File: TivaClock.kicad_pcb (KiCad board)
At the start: 2 copper layers, 6 parts, among them J1 Conn_01x10, J2 Conn_01x10, J3 Conn_01x10, J4 Conn_01x10, J5 Conn_01x20, J6 Conn_01x20

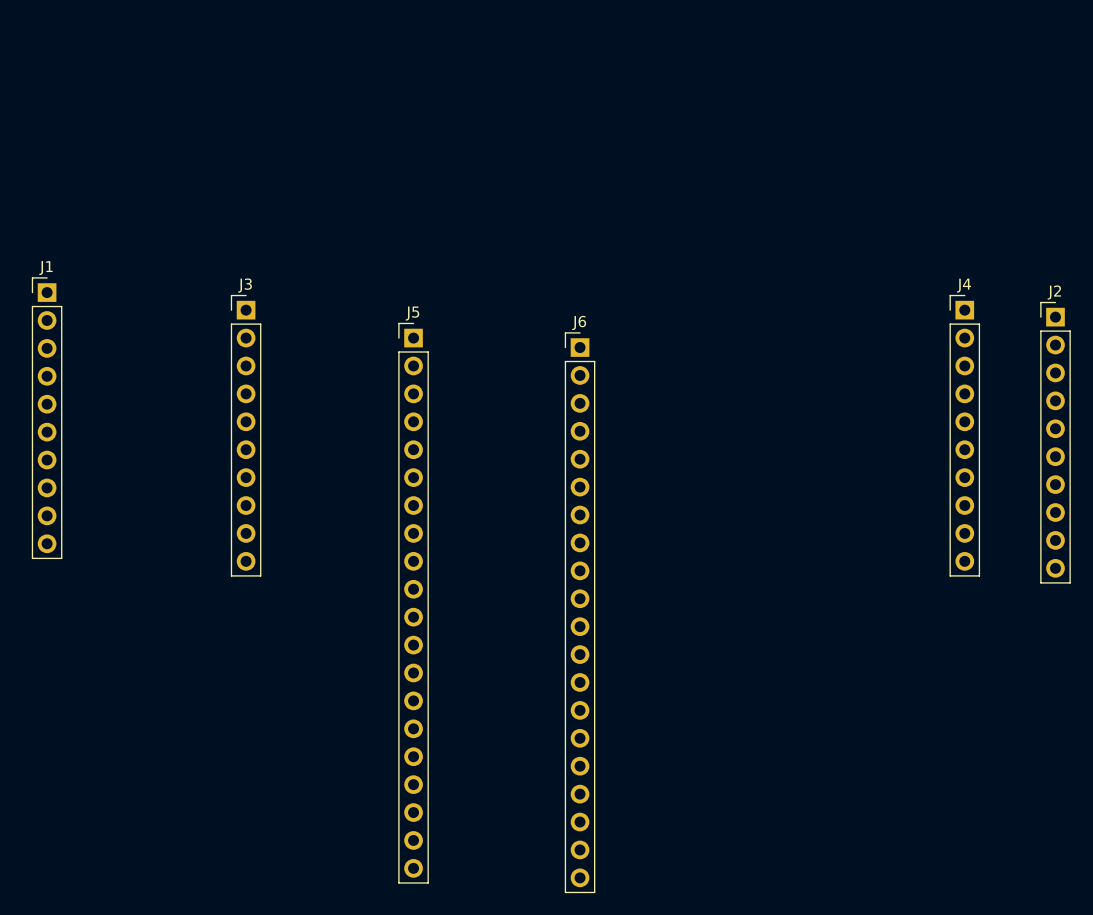
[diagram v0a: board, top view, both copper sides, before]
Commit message: added footprints and locations
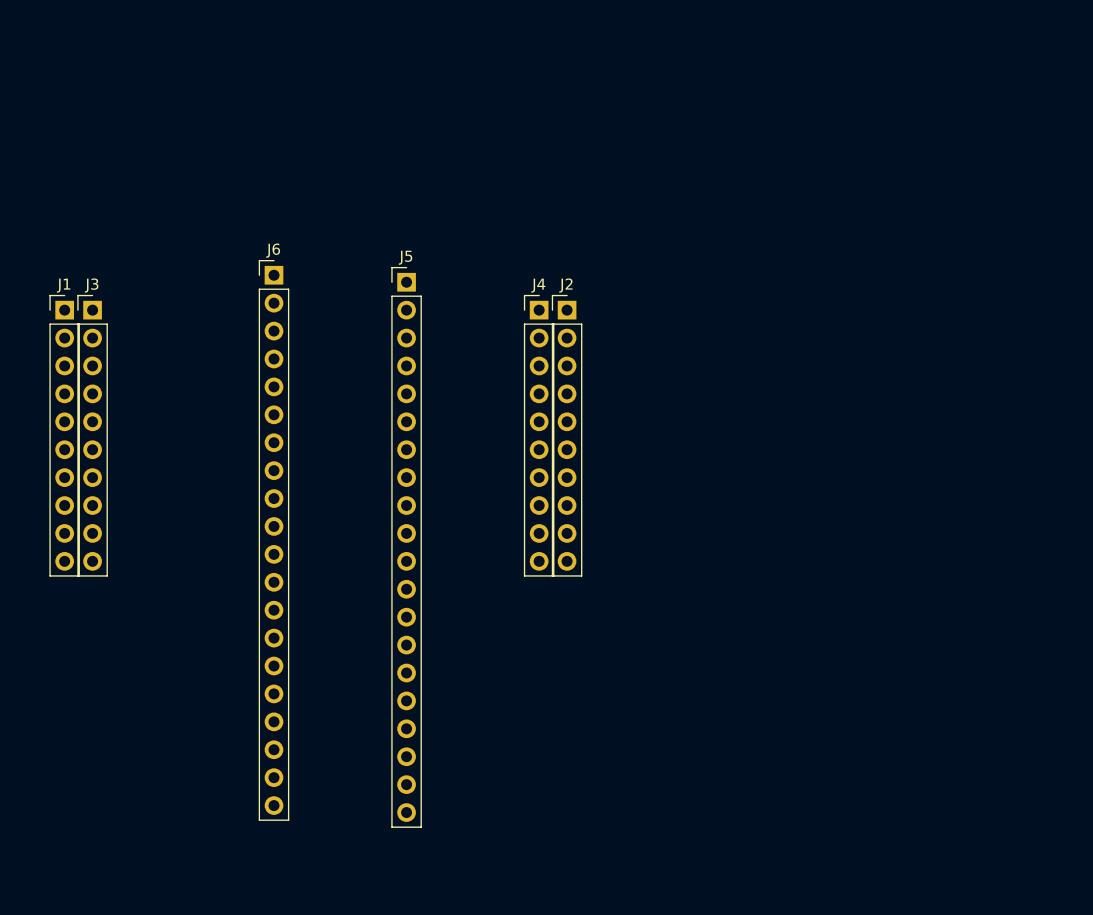
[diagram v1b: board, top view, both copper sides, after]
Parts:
- moved J2 44.5 mm to (147.3, 101.6)
- moved J4 38.7 mm to (144.8, 101.6)
- moved J6 28.6 mm to (120.7, 98.4)
- moved J3 14.0 mm to (104.1, 101.6)
- moved J5 5.12 mm to (132.7, 99.1)
- moved J1 2.26 mm to (101.6, 101.6)
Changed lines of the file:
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@@
   )
   (module Pin_Headers:Pin_Header_Straight_1x10_Pitch2.54mm (layer F.Cu)
-    (at 100 100)
+    (at 101.6 101.6)
     (descr "Through hole straight pin header, 1x10, 2.54mm pitch, single row")
     (tags "Through hole pin header THT 1x10 2.54mm single row")
@@
   )
   (module Pin_Headers:Pin_Header_Straight_1x10_Pitch2.54mm (layer F.Cu)
-    (at 191.77 102.235)
+    (at 147.32 101.6)
     (descr "Through hole straight pin header, 1x10, 2.54mm pitch, single row")
     (tags "Through hole pin header THT 1x10 2.54mm single row")
@@
   )
   (module Pin_Headers:Pin_Header_Straight_1x10_Pitch2.54mm (layer F.Cu)
-    (at 118.11 101.6)
+    (at 104.14 101.6)
     (descr "Through hole straight pin header, 1x10, 2.54mm pitch, single row")
     (tags "Through hole pin header THT 1x10 2.54mm single row")
@@
   )
   (module Pin_Headers:Pin_Header_Straight_1x10_Pitch2.54mm (layer F.Cu)
-    (at 183.515 101.6)
+    (at 144.78 101.6)
     (descr "Through hole straight pin header, 1x10, 2.54mm pitch, single row")
     (tags "Through hole pin header THT 1x10 2.54mm single row")
@@
   )
   (module Pin_Headers:Pin_Header_Straight_1x20_Pitch2.54mm (layer F.Cu)
-    (at 133.35 104.14)
+    (at 132.715 99.06)
     (descr "Through hole straight pin header, 1x20, 2.54mm pitch, single row")
     (tags "Through hole pin header THT 1x20 2.54mm single row")
@@
   )
   (module Pin_Headers:Pin_Header_Straight_1x20_Pitch2.54mm (layer F.Cu)
-    (at 148.5011 105.0036)
+    (at 120.65 98.425)
     (descr "Through hole straight pin header, 1x20, 2.54mm pitch, single row")
     (tags "Through hole pin header THT 1x20 2.54mm single row")

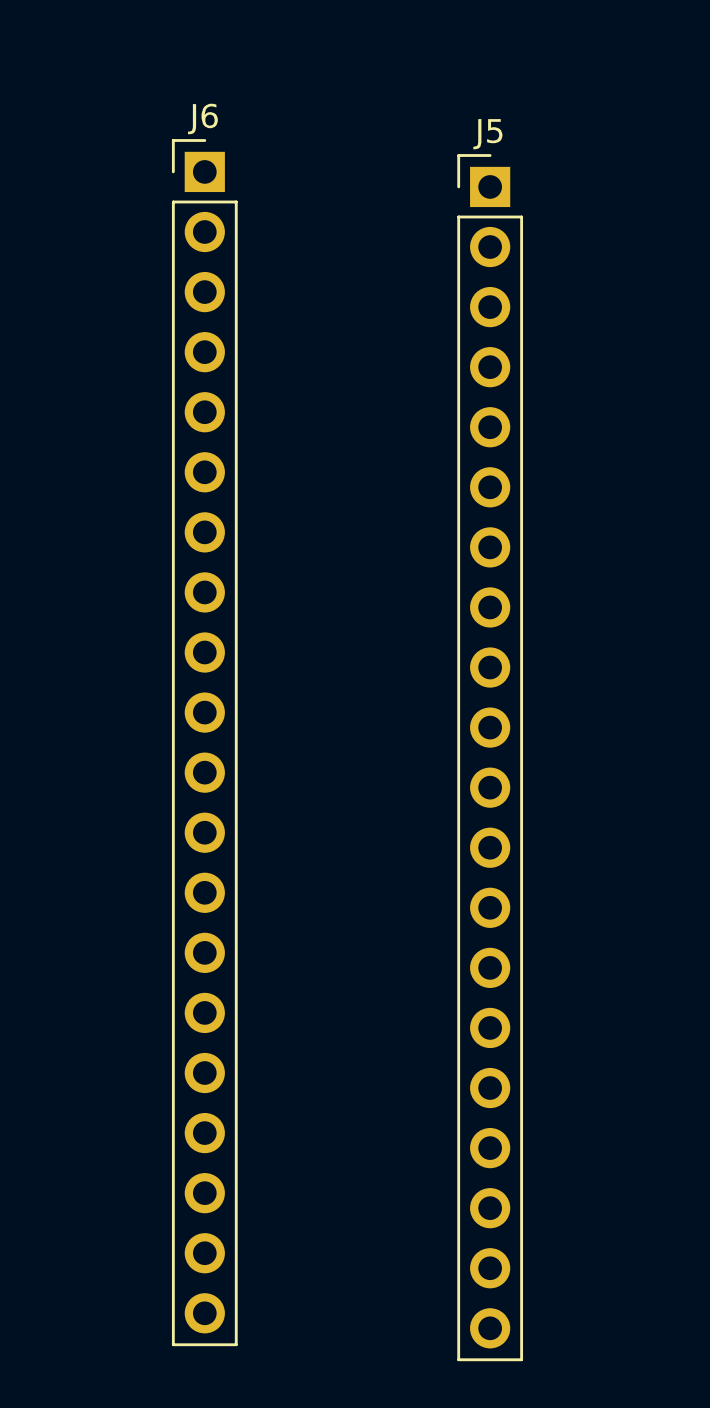
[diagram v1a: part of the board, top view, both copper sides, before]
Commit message: move clock micro to desired location
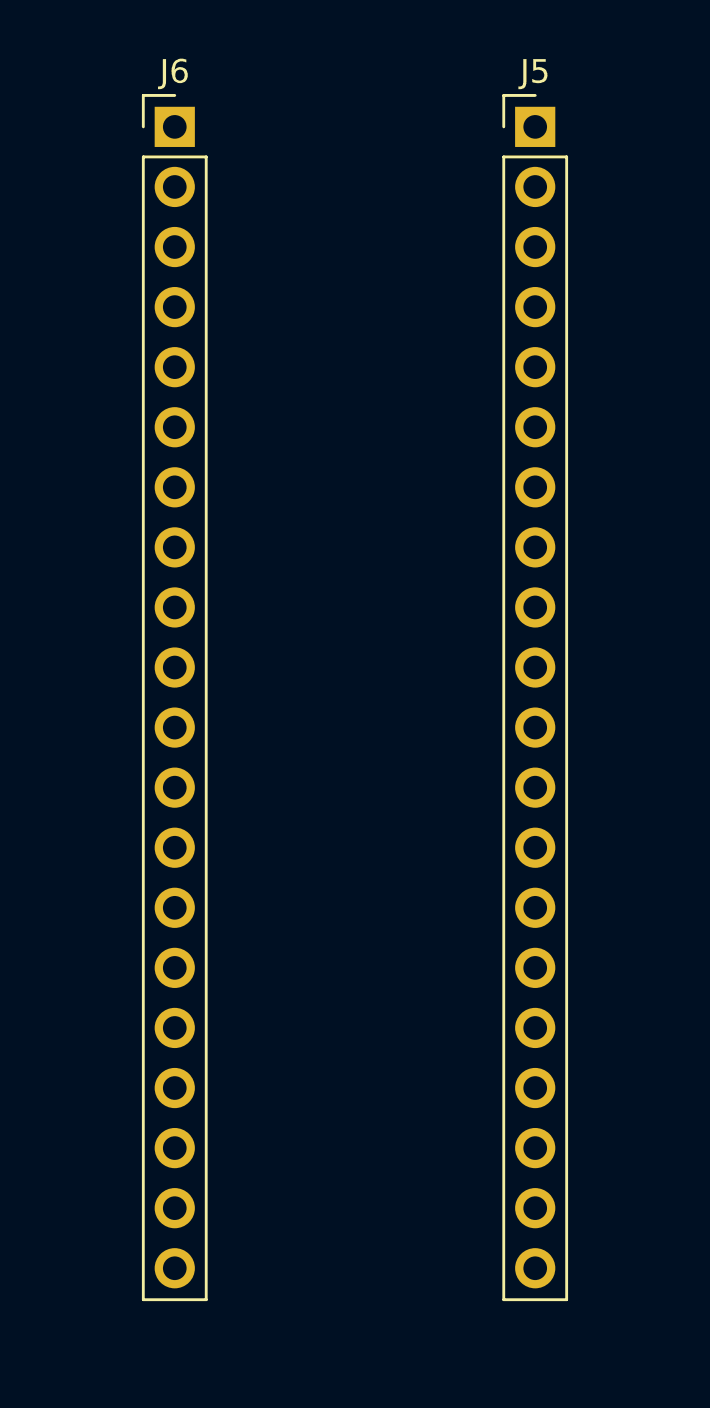
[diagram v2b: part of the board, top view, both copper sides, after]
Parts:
- moved J5 3.18 mm to (134.6, 96.5)
- moved J6 2.29 mm to (119.4, 96.5)
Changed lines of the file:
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@@
     (links 32)
     (no_connects 32)
-    (area 0 0 0 0)
+    (area 96.852381 95.12 152.06762 150.725)
     (thickness 1.6)
     (drawings 0)
@@
     (pad_to_mask_clearance 0.2)
     (aux_axis_origin 0 0)
+    (grid_origin 156.21 113.03)
     (visible_elements FFFFFF7F)
     (pcbplotparams
@@
   )
   (module Pin_Headers:Pin_Header_Straight_1x20_Pitch2.54mm (layer F.Cu)
-    (at 132.715 99.06)
+    (at 134.62 96.52)
     (descr "Through hole straight pin header, 1x20, 2.54mm pitch, single row")
     (tags "Through hole pin header THT 1x20 2.54mm single row")
@@
   )
   (module Pin_Headers:Pin_Header_Straight_1x20_Pitch2.54mm (layer F.Cu)
-    (at 120.65 98.425)
+    (at 119.38 96.52)
     (descr "Through hole straight pin header, 1x20, 2.54mm pitch, single row")
     (tags "Through hole pin header THT 1x20 2.54mm single row")

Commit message: orientate it corectly?
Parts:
- moved J5 30.5 mm to (134.6, 127.0), turned to 180 degrees
- moved J6 17.8 mm to (119.4, 78.7)
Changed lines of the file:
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@@
     (links 32)
     (no_connects 32)
-    (area 96.852381 95.12 152.06762 150.725)
+    (area 96.852381 75.435 152.06762 130.405)
     (thickness 1.6)
     (drawings 0)
@@
   )
   (module Pin_Headers:Pin_Header_Straight_1x20_Pitch2.54mm (layer F.Cu)
-    (at 134.62 96.52)
+    (at 134.62 127 180)
     (descr "Through hole straight pin header, 1x20, 2.54mm pitch, single row")
     (tags "Through hole pin header THT 1x20 2.54mm single row")
-    (fp_text reference J5 (at 0 -2.33) (layer F.SilkS)
-      (effects (font (size 1 1) (thickness 0.15)))
-    )
-    (fp_text value Conn_01x20 (at 0 50.59) (layer F.Fab)
+    (fp_text reference J5 (at 0 -2.33 180) (layer F.SilkS)
+      (effects (font (size 1 1) (thickness 0.15)))
+    )
+    (fp_text value Conn_01x20 (at 0 50.59 180) (layer F.Fab)
       (effects (font (size 1 1) (thickness 0.15)))
     )
@@
     (fp_line (start 1.8 50.05) (end 1.8 -1.8) (layer F.CrtYd) (width 0.05))
     (fp_line (start 1.8 -1.8) (end -1.8 -1.8) (layer F.CrtYd) (width 0.05))
-    (fp_text user %R (at 0 24.13 90) (layer F.Fab)
-      (effects (font (size 1 1) (thickness 0.15)))
-    )
-    (pad 1 thru_hole rect (at 0 0) (size 1.7 1.7) (drill 1) (layers *.Cu *.Mask)
+    (fp_text user %R (at 0 24.13 270) (layer F.Fab)
+      (effects (font (size 1 1) (thickness 0.15)))
+    )
+    (pad 1 thru_hole rect (at 0 0 180) (size 1.7 1.7) (drill 1) (layers *.Cu *.Mask)
       (net 24 /DS18B20))
-    (pad 2 thru_hole oval (at 0 2.54) (size 1.7 1.7) (drill 1) (layers *.Cu *.Mask)
+    (pad 2 thru_hole oval (at 0 2.54 180) (size 1.7 1.7) (drill 1) (layers *.Cu *.Mask)
       (net 36 /1302RST))
-    (pad 3 thru_hole oval (at 0 5.08) (size 1.7 1.7) (drill 1) (layers *.Cu *.Mask)
+    (pad 3 thru_hole oval (at 0 5.08 180) (size 1.7 1.7) (drill 1) (layers *.Cu *.Mask)
       (net 35 /1302IO))
-    (pad 4 thru_hole oval (at 0 7.62) (size 1.7 1.7) (drill 1) (layers *.Cu *.Mask)
+    (pad 4 thru_hole oval (at 0 7.62 180) (size 1.7 1.7) (drill 1) (layers *.Cu *.Mask)
       (net 34 /1302CLK))
-    (pad 5 thru_hole oval (at 0 10.16) (size 1.7 1.7) (drill 1) (layers *.Cu *.Mask)
+    (pad 5 thru_hole oval (at 0 10.16 180) (size 1.7 1.7) (drill 1) (layers *.Cu *.Mask)
       (net 33 /BEEP))
-    (pad 6 thru_hole oval (at 0 12.7) (size 1.7 1.7) (drill 1) (layers *.Cu *.Mask)
+    (pad 6 thru_hole oval (at 0 12.7 180) (size 1.7 1.7) (drill 1) (layers *.Cu *.Mask)
       (net 40 "Net-(J5-Pad6)"))
-    (pad 7 thru_hole oval (at 0 15.24) (size 1.7 1.7) (drill 1) (layers *.Cu *.Mask)
+    (pad 7 thru_hole oval (at 0 15.24 180) (size 1.7 1.7) (drill 1) (layers *.Cu *.Mask)
       (net 41 "Net-(J5-Pad7)"))
-    (pad 8 thru_hole oval (at 0 17.78) (size 1.7 1.7) (drill 1) (layers *.Cu *.Mask)
+    (pad 8 thru_hole oval (at 0 17.78 180) (size 1.7 1.7) (drill 1) (layers *.Cu *.Mask)
       (net 42 "Net-(J5-Pad8)"))
-    (pad 9 thru_hole oval (at 0 20.32) (size 1.7 1.7) (drill 1) (layers *.Cu *.Mask)
+    (pad 9 thru_hole oval (at 0 20.32 180) (size 1.7 1.7) (drill 1) (layers *.Cu *.Mask)
       (net 15 /RESET))
-    (pad 10 thru_hole oval (at 0 22.86) (size 1.7 1.7) (drill 1) (layers *.Cu *.Mask)
+    (pad 10 thru_hole oval (at 0 22.86 180) (size 1.7 1.7) (drill 1) (layers *.Cu *.Mask)
       (net 37 /RXD))
-    (pad 11 thru_hole oval (at 0 25.4) (size 1.7 1.7) (drill 1) (layers *.Cu *.Mask)
+    (pad 11 thru_hole oval (at 0 25.4 180) (size 1.7 1.7) (drill 1) (layers *.Cu *.Mask)
       (net 38 /TXD))
-    (pad 12 thru_hole oval (at 0 27.94) (size 1.7 1.7) (drill 1) (layers *.Cu *.Mask)
+    (pad 12 thru_hole oval (at 0 27.94 180) (size 1.7 1.7) (drill 1) (layers *.Cu *.Mask)
       (net 39 /MODE))
-    (pad 13 thru_hole oval (at 0 30.48) (size 1.7 1.7) (drill 1) (layers *.Cu *.Mask)
+    (pad 13 thru_hole oval (at 0 30.48 180) (size 1.7 1.7) (drill 1) (layers *.Cu *.Mask)
       (net 14 /PLUS))
-    (pad 14 thru_hole oval (at 0 33.02) (size 1.7 1.7) (drill 1) (layers *.Cu *.Mask)
+    (pad 14 thru_hole oval (at 0 33.02 180) (size 1.7 1.7) (drill 1) (layers *.Cu *.Mask)
       (net 18 /Bit8))
-    (pad 15 thru_hole oval (at 0 35.56) (size 1.7 1.7) (drill 1) (layers *.Cu *.Mask)
+    (pad 15 thru_hole oval (at 0 35.56 180) (size 1.7 1.7) (drill 1) (layers *.Cu *.Mask)
       (net 8 /Bit9))
-    (pad 16 thru_hole oval (at 0 38.1) (size 1.7 1.7) (drill 1) (layers *.Cu *.Mask)
+    (pad 16 thru_hole oval (at 0 38.1 180) (size 1.7 1.7) (drill 1) (layers *.Cu *.Mask)
       (net 9 /Bit10))
-    (pad 17 thru_hole oval (at 0 40.64) (size 1.7 1.7) (drill 1) (layers *.Cu *.Mask)
+    (pad 17 thru_hole oval (at 0 40.64 180) (size 1.7 1.7) (drill 1) (layers *.Cu *.Mask)
       (net 10 /Bit11))
-    (pad 18 thru_hole oval (at 0 43.18) (size 1.7 1.7) (drill 1) (layers *.Cu *.Mask)
+    (pad 18 thru_hole oval (at 0 43.18 180) (size 1.7 1.7) (drill 1) (layers *.Cu *.Mask)
       (net 43 "Net-(J5-Pad18)"))
-    (pad 19 thru_hole oval (at 0 45.72) (size 1.7 1.7) (drill 1) (layers *.Cu *.Mask)
+    (pad 19 thru_hole oval (at 0 45.72 180) (size 1.7 1.7) (drill 1) (layers *.Cu *.Mask)
       (net 44 "Net-(J5-Pad19)"))
-    (pad 20 thru_hole oval (at 0 48.26) (size 1.7 1.7) (drill 1) (layers *.Cu *.Mask)
+    (pad 20 thru_hole oval (at 0 48.26 180) (size 1.7 1.7) (drill 1) (layers *.Cu *.Mask)
       (net 11 /GND))
     (model ${KISYS3DMOD}/Pin_Headers.3dshapes/Pin_Header_Straight_1x20_Pitch2.54mm.wrl
@@
   )
   (module Pin_Headers:Pin_Header_Straight_1x20_Pitch2.54mm (layer F.Cu)
-    (at 119.38 96.52)
+    (at 119.38 78.74)
     (descr "Through hole straight pin header, 1x20, 2.54mm pitch, single row")
     (tags "Through hole pin header THT 1x20 2.54mm single row")

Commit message: autorouted
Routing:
- net /GND: track 0.00 -> 70.4 mm
- net /Bit11: track 0.00 -> 58.0 mm
- net /Bit9: track 0.00 -> 57.2 mm
- net /Bit10: track 0.00 -> 50.9 mm
- net /X2: track 0.00 -> 48.4 mm
- net /Bit7: track 0.00 -> 47.4 mm
- net /Bit6: track 0.00 -> 44.2 mm
- net /Bit0: track 0.00 -> 40.5 mm
- net /X0: track 0.00 -> 39.6 mm
- net /Bit3: track 0.00 -> 38.8 mm
- net /Bit2: track 0.00 -> 38.8 mm
- net /Bit1: track 0.00 -> 38.8 mm
- net /X3: track 0.00 -> 38.1 mm
- net /DS18B20: track 0.00 -> 38.0 mm
- net /X6: track 0.00 -> 36.6 mm
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
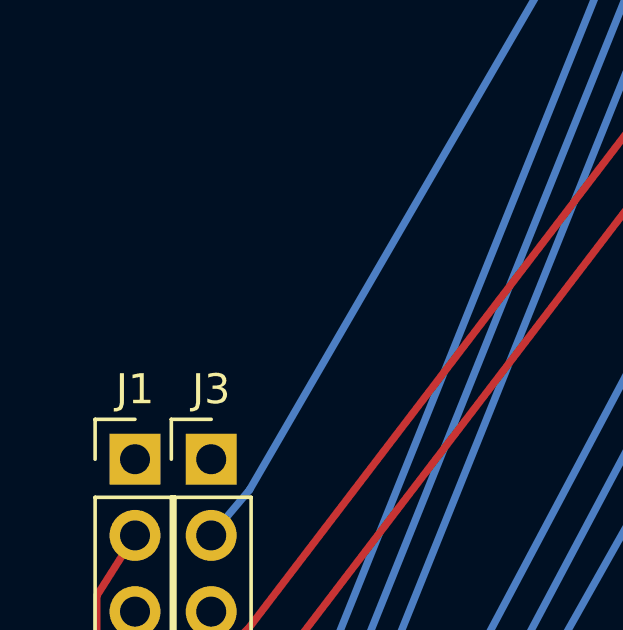
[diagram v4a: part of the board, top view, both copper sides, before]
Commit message: put solder jumper on PCB
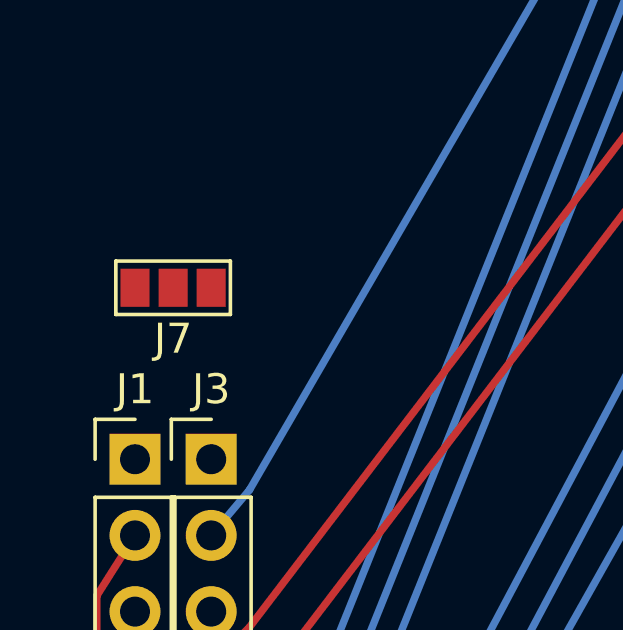
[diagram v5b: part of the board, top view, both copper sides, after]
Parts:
- added J7: GS3, Connectors:GS3, F.Cu at (102.9, 95.9)
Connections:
- J6 pad 11: Net-(J6-Pad11) -> /VCC
- J6 pad 20: Net-(J6-Pad20) -> /VCC
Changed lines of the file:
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@@
 (kicad_pcb (version 4) (host pcbnew 4.0.7)
   (general
-    (links 32)
-    (no_connects 32)
-    (area 96.852381 75.435 152.06762 130.405)
+    (links 36)
+    (no_connects 4)
+    (area 0 0 0 0)
     (thickness 1.6)
     (drawings 0)
     (tracks 325)
     (zones 0)
-    (modules 6)
-    (nets 49)
+    (modules 7)
+    (nets 48)
   )
   (page A4)
@@
   (net 45 "Net-(J6-Pad9)")
   (net 46 "Net-(J6-Pad10)")
-  (net 47 "Net-(J6-Pad11)")
-  (net 48 "Net-(J6-Pad20)")
+  (net 47 /VCC)
   (net_class Default "This is the default net class."
     (clearance 0.2)
@@
     (add_net /RXD)
     (add_net /TXD)
+    (add_net /VCC)
     (add_net /X0)
     (add_net /X1)
@@
     (add_net "Net-(J5-Pad8)")
     (add_net "Net-(J6-Pad10)")
-    (add_net "Net-(J6-Pad11)")
-    (add_net "Net-(J6-Pad20)")
     (add_net "Net-(J6-Pad9)")
   )
@@
       (net 46 "Net-(J6-Pad10)"))
     (pad 11 thru_hole oval (at 0 25.4) (size 1.7 1.7) (drill 1) (layers *.Cu *.Mask)
-      (net 47 "Net-(J6-Pad11)"))
+      (net 47 /VCC))
     (pad 12 thru_hole oval (at 0 27.94) (size 1.7 1.7) (drill 1) (layers *.Cu *.Mask)
       (net 16 /X7))
@@
       (net 3 /X0))
     (pad 20 thru_hole oval (at 0 48.26) (size 1.7 1.7) (drill 1) (layers *.Cu *.Mask)
-      (net 48 "Net-(J6-Pad20)"))
+      (net 47 /VCC))
     (model ${KISYS3DMOD}/Pin_Headers.3dshapes/Pin_Header_Straight_1x20_Pitch2.54mm.wrl
       (at (xyz 0 0 0))
@@
     )
   )
+  (module Connectors:GS3 (layer F.Cu)
+    (at 102.87 95.885 90)
+    (descr "3-pin solder bridge")
+    (tags "solder bridge")
+    (attr smd)
+    (fp_text reference J7 (at -1.7 0 180) (layer F.SilkS)
+      (effects (font (size 1 1) (thickness 0.15)))
+    )
+    (fp_text value GS3 (at 1.8 0 180) (layer F.Fab)
+      (effects (font (size 1 1) (thickness 0.15)))
+    )
+    (fp_line (start -1.15 -2.15) (end 1.15 -2.15) (layer F.CrtYd) (width 0.05))
+    (fp_line (start 1.15 -2.15) (end 1.15 2.15) (layer F.CrtYd) (width 0.05))
+    (fp_line (start 1.15 2.15) (end -1.15 2.15) (layer F.CrtYd) (width 0.05))
+    (fp_line (start -1.15 2.15) (end -1.15 -2.15) (layer F.CrtYd) (width 0.05))
+    (fp_line (start -0.89 -1.91) (end -0.89 1.91) (layer F.SilkS) (width 0.12))
+    (fp_line (start -0.89 1.91) (end 0.89 1.91) (layer F.SilkS) (width 0.12))
+    (fp_line (start 0.89 1.91) (end 0.89 -1.91) (layer F.SilkS) (width 0.12))
+    (fp_line (start -0.89 -1.91) (end 0.89 -1.91) (layer F.SilkS) (width 0.12))
+    (pad 1 smd rect (at 0 -1.27 90) (size 1.27 0.97) (layers F.Cu F.Paste F.Mask)
+      (net 1 "Net-(J1-Pad1)"))
+    (pad 2 smd rect (at 0 0 90) (size 1.27 0.97) (layers F.Cu F.Paste F.Mask)
+      (net 47 /VCC))
+    (pad 3 smd rect (at 0 1.27 90) (size 1.27 0.97) (layers F.Cu F.Paste F.Mask)
+      (net 21 "Net-(J3-Pad1)"))
+  )
   (segment (start 100.3272 106.1495) (end 101.6 104.14) (width 0.25) (layer F.Cu) (net 2))
